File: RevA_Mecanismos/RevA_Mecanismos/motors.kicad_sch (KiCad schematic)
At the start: 47 parts, among them J10 430450224, J11 430450224, J12 Conn_01x08_Socket, J13 Conn_01x08_Socket, J14 Conn_01x02_Pin, J15 430450624, J20 3557-2, J21 Conn_01x04_Pin, J22 Conn_01x04_Pin, J8 3557-2, J9 3557-2, Q3 IRF9540NSPBF, Q4 IRF9540NSPBF, Q5 IRF9540NSPBF, Q6 IRF9540NSPBF, U4 IRF540SPBF, U5 IRF540SPBF, U6 IRF540SPBF, U7 IRF540SPBF, U8 TXB0104D

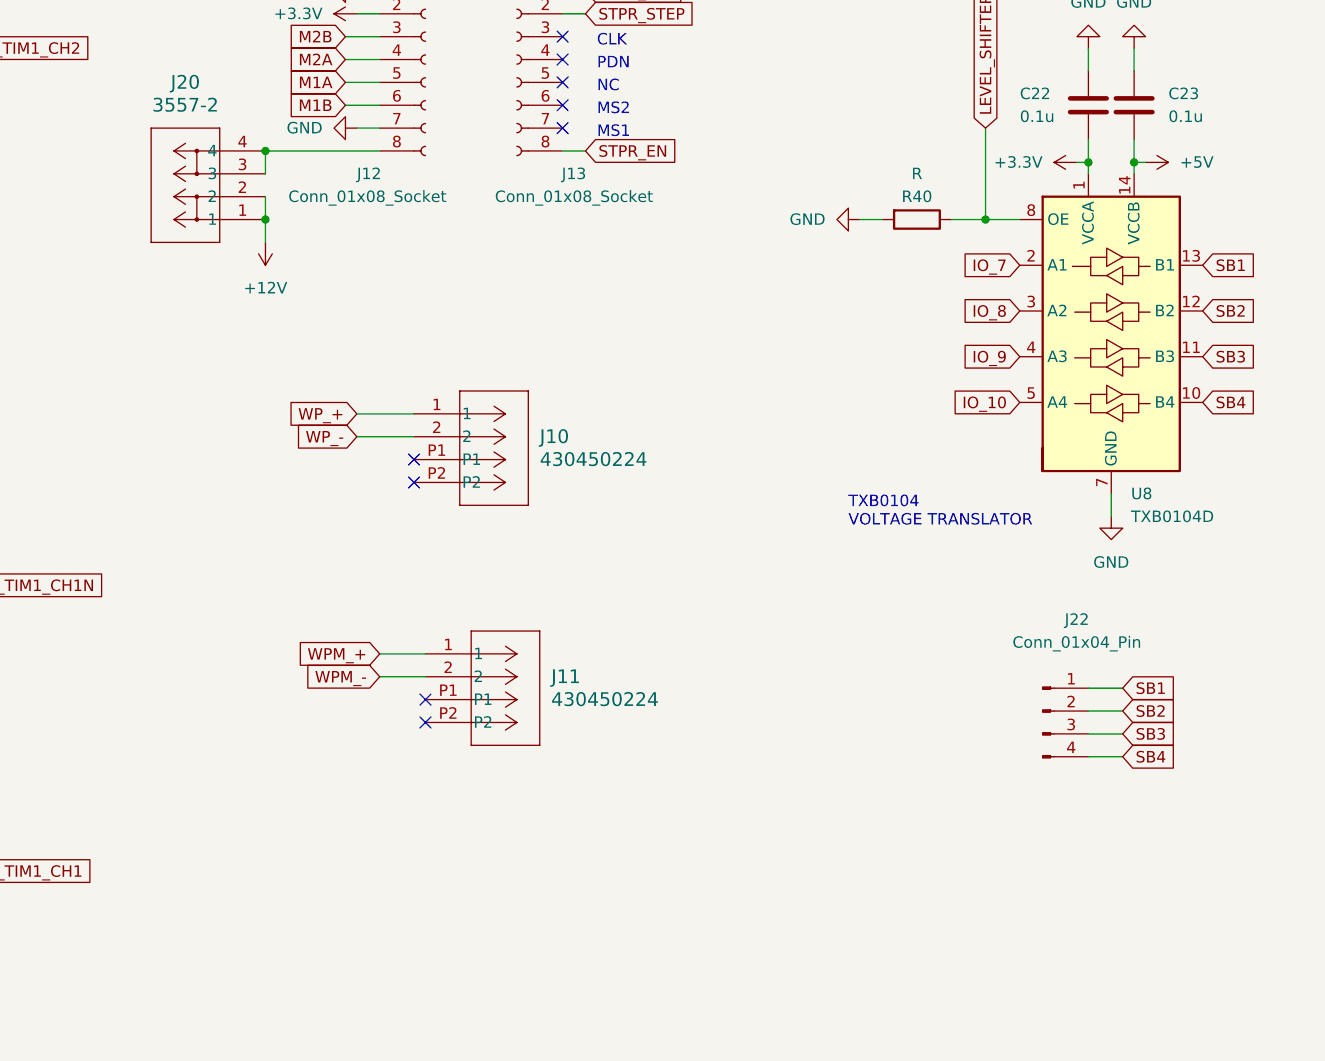
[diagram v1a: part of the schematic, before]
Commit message: Corrections to component footprints in schematic design made during the development of BOM
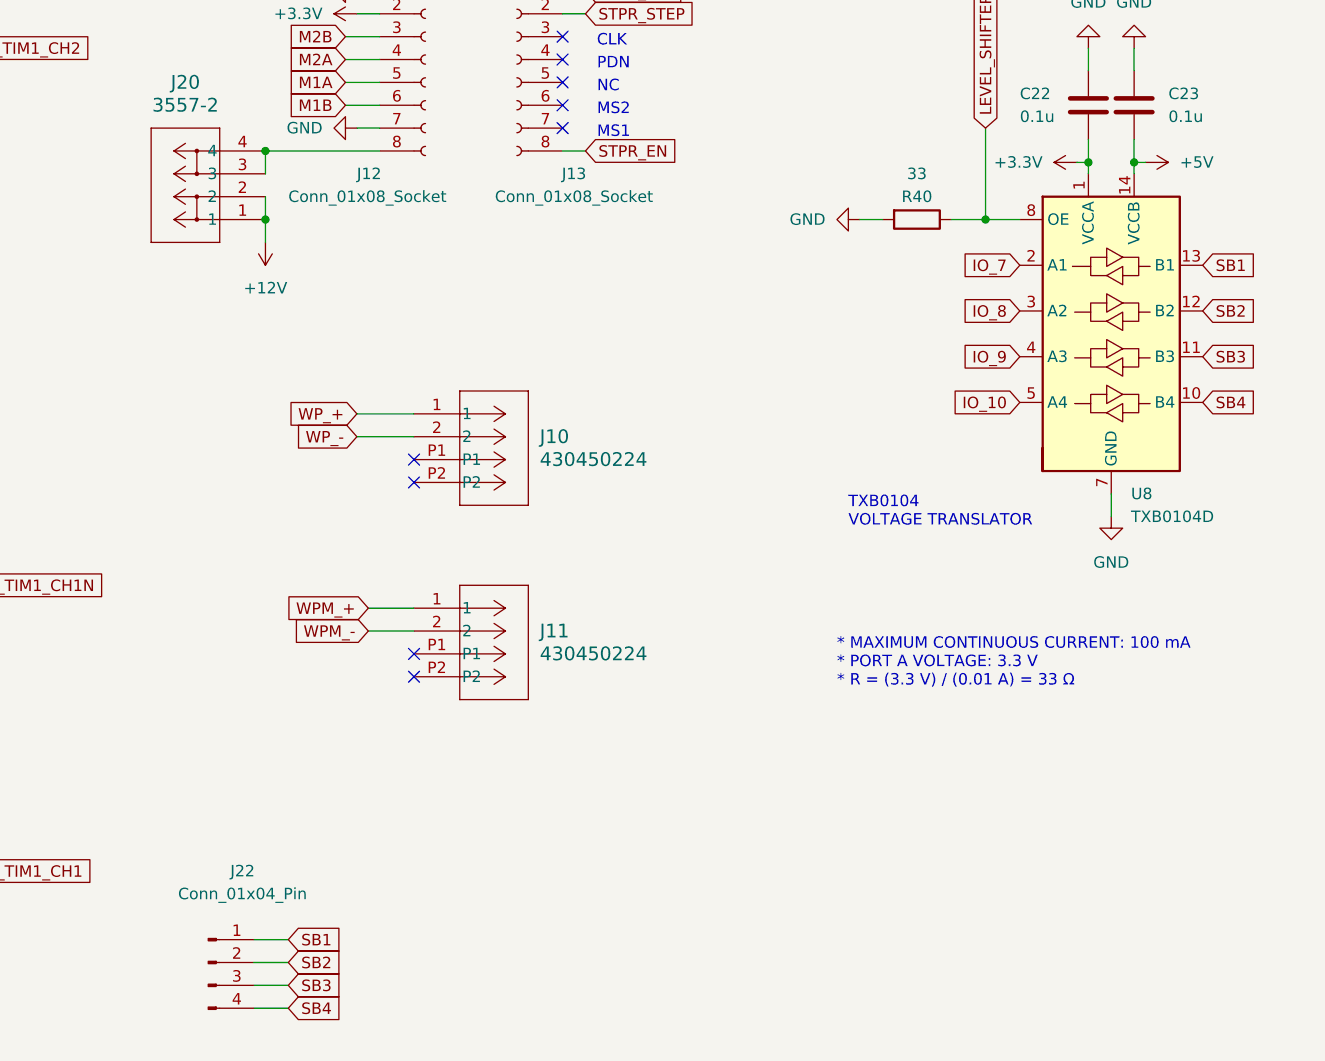
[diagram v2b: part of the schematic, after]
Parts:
- J21: footprint TerminalBlock:TerminalBlock_Altech_AK300-2_P5.00mm -> Connector_PinHeader_2.54mm:PinHeader_1x04_P2.54mm_Vertical
- J22: footprint Connector_PinHeader_2.54mm:PinHeader_1x02_P2.54mm_Vertical -> Connector_PinHeader_2.54mm:PinHeader_1x04_P2.54mm_Vertical
- R40: value R -> 33
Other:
- note added: "* MAXIMUM CONTINUOUS CURRENT: 100 mA * PORT A VOLTAGE: 3.3 V * R = (3.3 V) / (0.01 A) = 33 Ω"
- moved on the sheet: J11, J22
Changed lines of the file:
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@@
   (no_connect (at 180.34 125.73))
   (no_connect (at 180.34 128.27))
-  (no_connect (at 181.61 154.94))
+  (no_connect (at 180.34 149.86))
   (no_connect (at 196.85 81.28))
   (no_connect (at 196.85 86.36))
@@
   (no_connect (at 196.85 88.9))
   (no_connect (at 196.85 78.74))
-  (no_connect (at 181.61 152.4))
+  (no_connect (at 180.34 147.32))
   (wire (pts (xy 76.2 176.53) (xy 76.2 181.61))
     (stroke (width 0) (type default))
@@
     (stroke (width 0) (type default))
   )
-  (wire (pts (xy 255.27 153.67) (xy 259.08 153.67))
+  (wire (pts (xy 162.56 181.61) (xy 166.37 181.61))
     (stroke (width 0) (type default))
   )
@@
     (stroke (width 0) (type default))
   )
-  (wire (pts (xy 255.27 151.13) (xy 259.08 151.13))
+  (wire (pts (xy 162.56 179.07) (xy 166.37 179.07))
     (stroke (width 0) (type default))
   )
@@
     (stroke (width 0) (type default))
   )
-  (wire (pts (xy 255.27 158.75) (xy 259.08 158.75))
+  (wire (pts (xy 162.56 186.69) (xy 166.37 186.69))
     (stroke (width 0) (type default))
   )
@@
     (stroke (width 0) (type default))
   )
-  (wire (pts (xy 181.61 147.32) (xy 176.53 147.32))
+  (wire (pts (xy 180.34 142.24) (xy 175.26 142.24))
     (stroke (width 0) (type default))
   )
@@
     (stroke (width 0) (type default))
   )
-  (wire (pts (xy 255.27 156.21) (xy 259.08 156.21))
+  (wire (pts (xy 162.56 184.15) (xy 166.37 184.15))
     (stroke (width 0) (type default))
   )
@@
     (stroke (width 0) (type default))
   )
-  (wire (pts (xy 181.61 149.86) (xy 176.53 149.86))
+  (wire (pts (xy 180.34 144.78) (xy 175.26 144.78))
     (stroke (width 0) (type default))
   )
@@
   )
   (text "WATERPROOF MOTOR H-BRIDGE" (at 48.26 123.19 0)
+    (effects (font (size 1.27 1.27)) (justify left bottom))
+  )
+  (text "* MAXIMUM CONTINUOUS CURRENT: 100 mA\n* PORT A VOLTAGE: 3.3 V\n* R = (3.3 V) / (0.01 A) = 33 Ω"
+    (at 227.33 151.13 0)
     (effects (font (size 1.27 1.27)) (justify left bottom))
   )
@@
     )
   )
-  (global_label "SB3" (shape input) (at 259.08 156.21 0) (fields_autoplaced)
+  (global_label "SB3" (shape input) (at 166.37 184.15 0) (fields_autoplaced)
     (effects (font (size 1.27 1.27)) (justify left))
-    (property "Intersheetrefs" "${INTERSHEET_REFS}" (at 265.7542 156.21 0)
+    (property "Intersheetrefs" "${INTERSHEET_REFS}" (at 173.0442 184.15 0)
       (effects (font (size 1.27 1.27)) (justify left) hide)
     )
   )
-  (global_label "SB1" (shape input) (at 259.08 151.13 0) (fields_autoplaced)
+  (global_label "SB1" (shape input) (at 166.37 179.07 0) (fields_autoplaced)
     (effects (font (size 1.27 1.27)) (justify left))
-    (property "Intersheetrefs" "${INTERSHEET_REFS}" (at 265.7542 151.13 0)
+    (property "Intersheetrefs" "${INTERSHEET_REFS}" (at 173.0442 179.07 0)
       (effects (font (size 1.27 1.27)) (justify left) hide)
     )
@@
     )
   )
-  (global_label "SB4" (shape input) (at 259.08 158.75 0) (fields_autoplaced)
+  (global_label "SB4" (shape input) (at 166.37 186.69 0) (fields_autoplaced)
     (effects (font (size 1.27 1.27)) (justify left))
-    (property "Intersheetrefs" "${INTERSHEET_REFS}" (at 265.7542 158.75 0)
+    (property "Intersheetrefs" "${INTERSHEET_REFS}" (at 173.0442 186.69 0)
       (effects (font (size 1.27 1.27)) (justify left) hide)
     )
@@
     )
   )
-  (global_label "SB2" (shape input) (at 259.08 153.67 0) (fields_autoplaced)
+  (global_label "SB2" (shape input) (at 166.37 181.61 0) (fields_autoplaced)
     (effects (font (size 1.27 1.27)) (justify left))
-    (property "Intersheetrefs" "${INTERSHEET_REFS}" (at 265.7542 153.67 0)
+    (property "Intersheetrefs" "${INTERSHEET_REFS}" (at 173.0442 181.61 0)
       (effects (font (size 1.27 1.27)) (justify left) hide)
     )
@@
     )
   )
-  (global_label "WPM_+" (shape input) (at 176.53 147.32 180)
+  (global_label "WPM_+" (shape input) (at 175.26 142.24 180)
     (effects (font (size 1.27 1.27)) (justify right))
-    (property "Intersheetrefs" "${INTERSHEET_REFS}" (at 165.4567 147.2406 0)
+    (property "Intersheetrefs" "${INTERSHEET_REFS}" (at 164.1867 142.1606 0)
       (effects (font (size 1.27 1.27)) (justify right) hide)
     )
   )
-  (global_label "WPM_-" (shape input) (at 176.53 149.86 180)
+  (global_label "WPM_-" (shape input) (at 175.26 144.78 180)
     (effects (font (size 1.27 1.27)) (justify right))
-    (property "Intersheetrefs" "${INTERSHEET_REFS}" (at 165.4567 149.7806 0)
+    (property "Intersheetrefs" "${INTERSHEET_REFS}" (at 164.1867 144.7006 0)
       (effects (font (size 1.27 1.27)) (justify right) hide)
     )
@@
       (effects (font (size 1.27 1.27) italic) hide)
     )
-    (property "Datasheet" "IRF540SPBF" (at 57.15 80.01 0)
+    (property "Datasheet" "https://www.vishay.com/docs/91022/sihf540s.pdf" (at 57.15 80.01 0)
       (effects (font (size 1.27 1.27) italic) hide)
     )
@@
       (effects (font (size 1.27 1.27) italic) hide)
     )
-    (property "Datasheet" "IRF540SPBF" (at 110.49 171.45 0)
+    (property "Datasheet" "https://www.vishay.com/docs/91022/sihf540s.pdf" (at 110.49 171.45 0)
       (effects (font (size 1.27 1.27) italic) hide)
     )
@@
       (effects (font (size 1.27 1.27) italic) hide)
     )
-    (property "Datasheet" "IRF9540NSPBF" (at 110.49 139.7 0)
+    (property "Datasheet" "https://www.mouser.mx/datasheet/2/196/irf9540nspbf-1228169.pdf" (at 110.49 139.7 0)
       (effects (font (size 1.27 1.27) italic) hide)
     )
@@
     )
   )
-  (symbol (lib_id "Connector:Conn_01x04_Pin") (at 250.19 153.67 0) (unit 1)
-    (in_bom yes) (on_board yes) (dnp no)
-    (property "Reference" "J22" (at 254 143.51 0)
+  (symbol (lib_id "Connector:Conn_01x04_Pin") (at 157.48 181.61 0) (unit 1)
+    (in_bom yes) (on_board yes) (dnp no)
+    (property "Reference" "J22" (at 161.29 171.45 0)
       (effects (font (size 1.27 1.27)))
     )
-    (property "Value" "Conn_01x04_Pin" (at 254 146.05 0)
+    (property "Value" "Conn_01x04_Pin" (at 161.29 173.99 0)
       (effects (font (size 1.27 1.27)))
     )
-    (property "Footprint" "Connector_PinHeader_2.54mm:PinHeader_1x02_P2.54mm_Vertical" (at 250.19 153.67 0)
-      (effects (font (size 1.27 1.27)) hide)
-    )
-    (property "Datasheet" "~" (at 250.19 153.67 0)
+    (property "Footprint" "Connector_PinHeader_2.54mm:PinHeader_1x04_P2.54mm_Vertical" (at 157.48 181.61 0)
+      (effects (font (size 1.27 1.27)) hide)
+    )
+    (property "Datasheet" "~" (at 157.48 181.61 0)
       (effects (font (size 1.27 1.27)) hide)
     )
@@
       (effects (font (size 1.27 1.27) italic) hide)
     )
-    (property "Datasheet" "IRF9540NSPBF" (at 57.15 48.26 0)
+    (property "Datasheet" "https://www.mouser.mx/datasheet/2/196/irf9540nspbf-1228169.pdf" (at 57.15 48.26 0)
       (effects (font (size 1.27 1.27) italic) hide)
     )
@@
       (effects (font (size 1.27 1.27) italic) hide)
     )
-    (property "Datasheet" "IRF540SPBF" (at 110.49 80.01 0)
+    (property "Datasheet" "https://www.vishay.com/docs/91022/sihf540s.pdf" (at 110.49 80.01 0)
       (effects (font (size 1.27 1.27) italic) hide)
     )
@@
       (effects (font (size 1.27 1.27)))
     )
-    (property "Footprint" "TerminalBlock:TerminalBlock_Altech_AK300-2_P5.00mm" (at 173.99 52.07 0)
+    (property "Footprint" "Connector_PinHeader_2.54mm:PinHeader_1x04_P2.54mm_Vertical" (at 173.99 52.07 0)
       (effects (font (size 1.27 1.27)) hide)
     )
@@
       (effects (font (size 1.27 1.27)))
     )
-    (property "Value" "R" (at 236.22 93.98 90)
+    (property "Value" "33" (at 236.22 93.98 90)
       (effects (font (size 1.27 1.27)))
     )
@@
       (effects (font (size 1.27 1.27) italic) hide)
     )
-    (property "Datasheet" "IRF9540NSPBF" (at 57.15 139.7 0)
+    (property "Datasheet" "https://www.mouser.mx/datasheet/2/196/irf9540nspbf-1228169.pdf" (at 57.15 139.7 0)
       (effects (font (size 1.27 1.27) italic) hide)
     )
@@
       (effects (font (size 1.27 1.27) italic) hide)
     )
-    (property "Datasheet" "IRF9540NSPBF" (at 110.49 48.26 0)
+    (property "Datasheet" "https://www.mouser.mx/datasheet/2/196/irf9540nspbf-1228169.pdf" (at 110.49 48.26 0)
       (effects (font (size 1.27 1.27) italic) hide)
     )
@@
     )
   )
-  (symbol (lib_id "MolexConnectors:430450224") (at 181.61 147.32 0) (unit 1)
-    (in_bom yes) (on_board yes) (dnp no) (fields_autoplaced)
-    (property "Reference" "J11" (at 195.58 149.86 0)
+  (symbol (lib_id "MolexConnectors:430450224") (at 180.34 142.24 0) (unit 1)
+    (in_bom yes) (on_board yes) (dnp no) (fields_autoplaced)
+    (property "Reference" "J11" (at 194.31 144.78 0)
       (effects (font (size 1.524 1.524)) (justify left))
     )
-    (property "Value" "430450224" (at 195.58 152.4 0)
+    (property "Value" "430450224" (at 194.31 147.32 0)
       (effects (font (size 1.524 1.524)) (justify left))
     )
-    (property "Footprint" "MolexConnectors:CON_430450224_MOL" (at 181.61 147.32 0)
+    (property "Footprint" "MolexConnectors:CON_430450224_MOL" (at 180.34 142.24 0)
       (effects (font (size 1.27 1.27) italic) hide)
     )
-    (property "Datasheet" "430450224" (at 181.61 147.32 0)
+    (property "Datasheet" "430450224" (at 180.34 142.24 0)
       (effects (font (size 1.27 1.27) italic) hide)
     )
@@
       (effects (font (size 1.27 1.27) italic) hide)
     )
-    (property "Datasheet" "IRF540SPBF" (at 57.15 171.45 0)
+    (property "Datasheet" "https://www.vishay.com/docs/91022/sihf540s.pdf" (at 57.15 171.45 0)
       (effects (font (size 1.27 1.27) italic) hide)
     )
